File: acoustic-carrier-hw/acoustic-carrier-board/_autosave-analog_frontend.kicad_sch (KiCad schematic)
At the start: 47 parts, among them J1 8P8C_Shielded, U2 THS4521IDGK, U3 DGQ2788AEN-T1-GE4, U5 LMV321

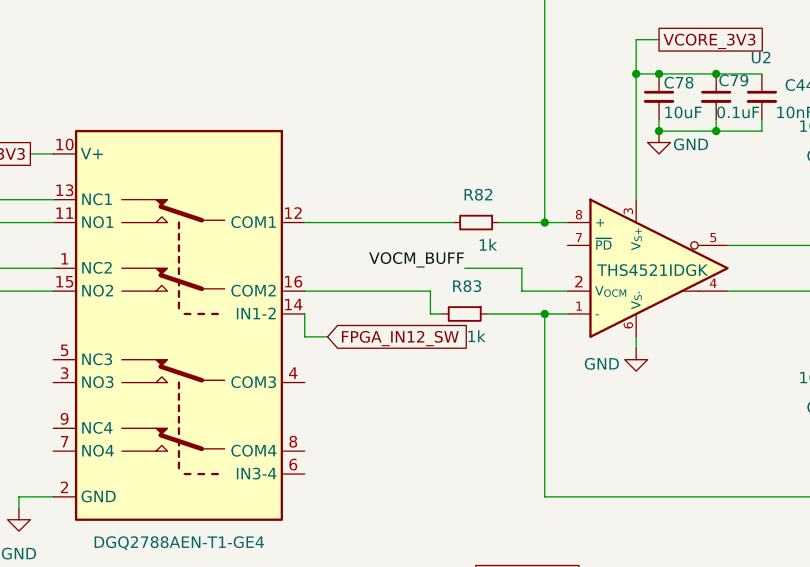
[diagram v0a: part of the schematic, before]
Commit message: [carrier] Added switch (next) add appropriate test point on secondary dpdt
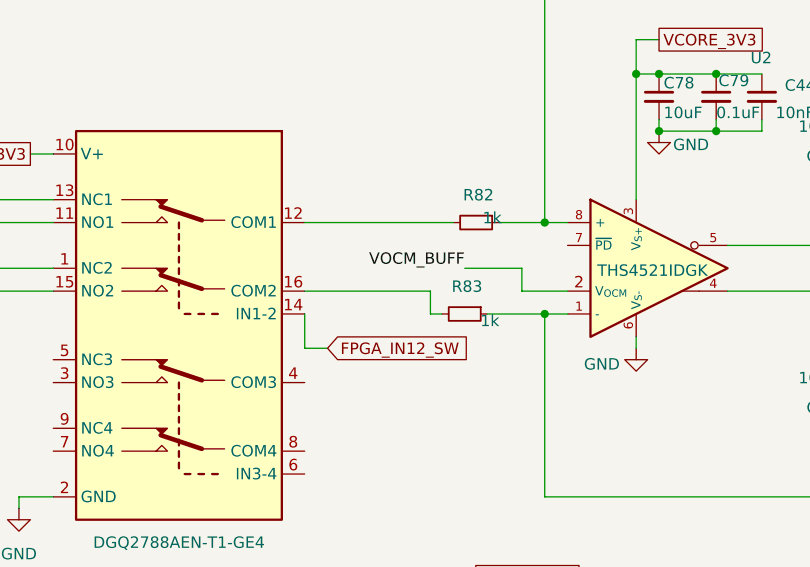
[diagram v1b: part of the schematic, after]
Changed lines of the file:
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@@
 	(wire
 		(pts
-			(xy 138.43 78.74) (xy 135.89 78.74)
+			(xy 138.43 80.01) (xy 135.89 80.01)
 		)
 		(stroke
@@
 	(wire
 		(pts
-			(xy 135.89 78.74) (xy 135.89 76.2)
+			(xy 135.89 80.01) (xy 135.89 76.2)
 		)
 		(stroke
@@
 	(global_label "FPGA_IN12_SW"
 		(shape input)
-		(at 138.43 78.74 0)
+		(at 138.43 80.01 0)
 		(fields_autoplaced yes)
 		(effects
@@
 		)
 		(property "Intersheetrefs" "${INTERSHEET_REFS}"
-			(at 155.0828 78.74 0)
+			(at 155.0828 80.01 0)
 			(effects
 				(font
@@
 		)
 		(property "Value" "1k"
-			(at 154.94 78.74 90)
+			(at 156.464 76.962 90)
 			(effects
 				(font
@@
 		)
 		(property "Value" "1k"
-			(at 156.21 68.58 90)
+			(at 156.718 65.532 90)
 			(effects
 				(font
